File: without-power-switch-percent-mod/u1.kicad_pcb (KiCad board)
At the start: 2 copper layers, 18 x 16.5 mm, 12 parts, among them J1 USB_C_Receptacle_USB2.0, J2 Conn_01x06_MountingPin, U1 USBLC6-2P6

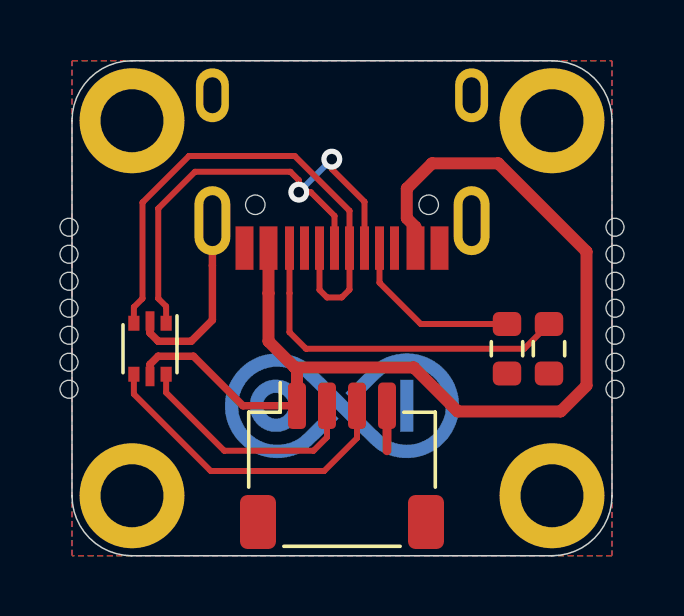
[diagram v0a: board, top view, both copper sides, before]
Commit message: Update Percent Mod KiCad project version
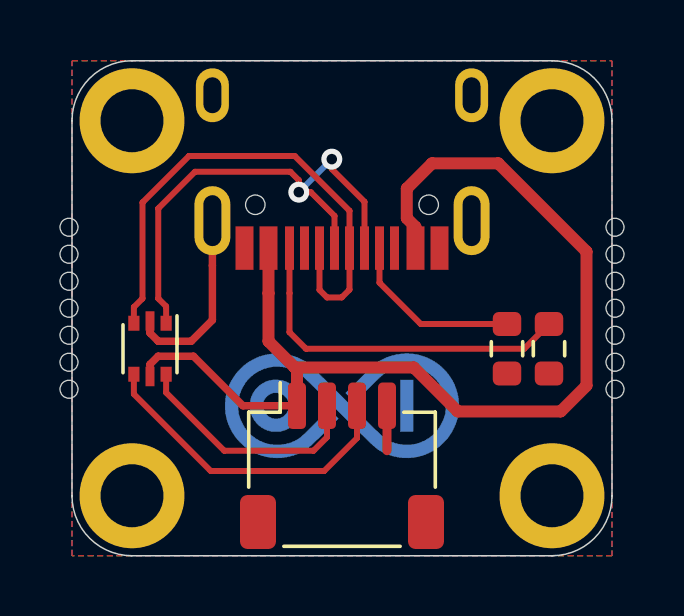
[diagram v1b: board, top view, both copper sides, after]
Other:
- net class Default removed
